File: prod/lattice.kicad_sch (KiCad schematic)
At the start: 65 parts, among them J1 USB_C_Receptacle, J2 USB_C_Receptacle, J3 AudioJack4, U1 XC6206PxxxMR, U2 USBLC6-2SC6, U3 CH552T

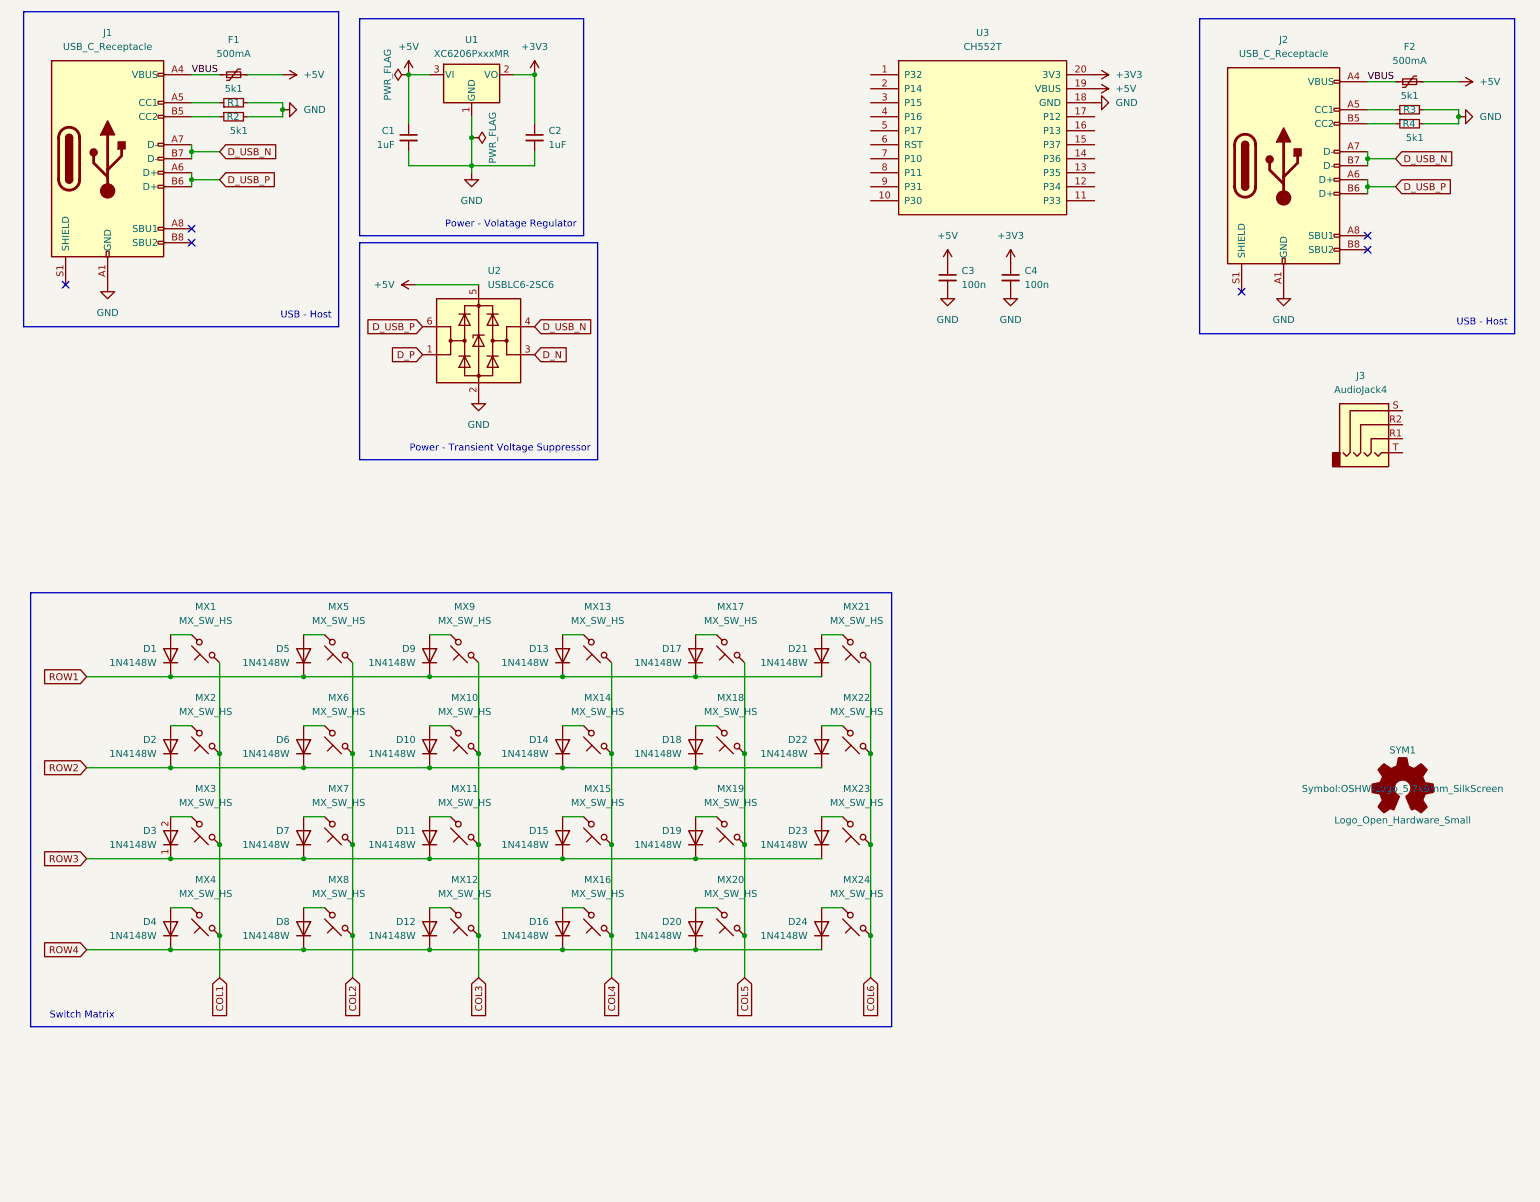
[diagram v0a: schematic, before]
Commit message: more complete schematic
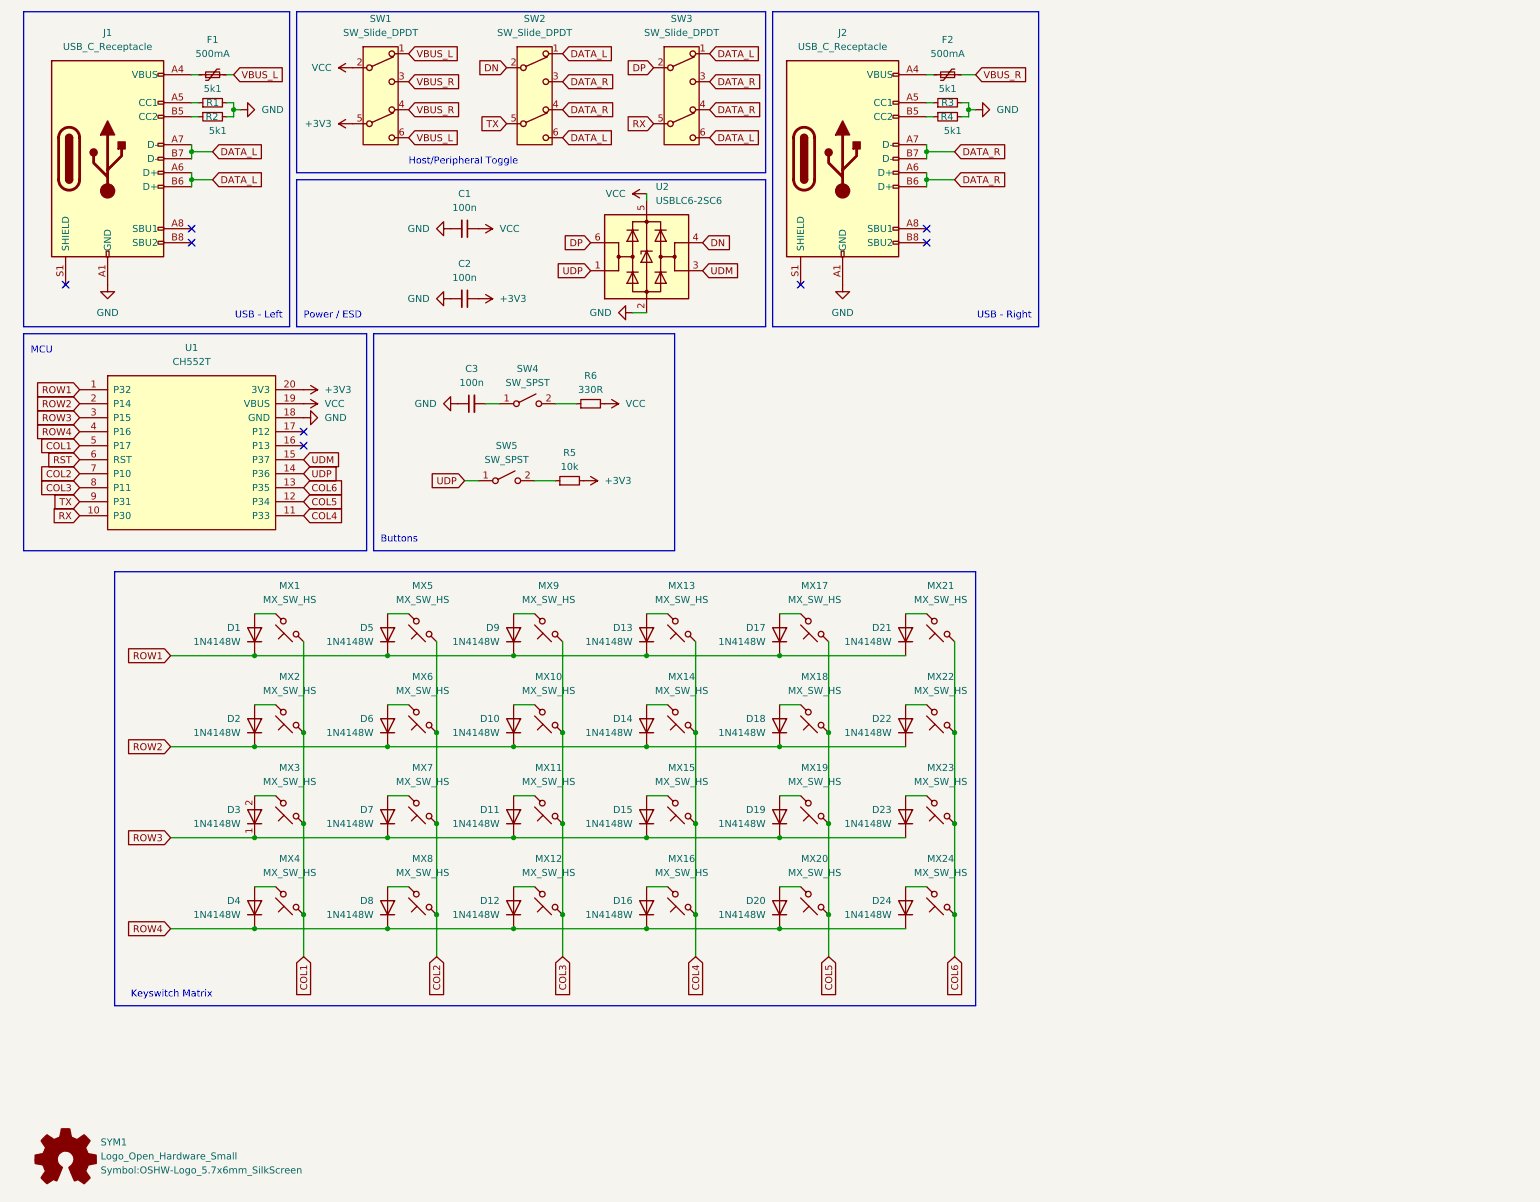
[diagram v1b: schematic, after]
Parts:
- removed C1, C2: 1uF, Capacitor_SMD:C_0402_1005Metric, symbol Device:C_Small
- removed J3: AudioJack4, symbol Connector_Audio:AudioJack4
- removed U1: XC6206PxxxMR, lattice:SOT-23-3, symbol Regulator_Linear:XC6206PxxxMR
- added C3: 100n, symbol Device:C_Small
- added R5: 10k, symbol Device:R_Small
- added R6: 330R, symbol Device:R_Small
- added SW1, SW2, SW3: SW_Slide_DPDT, symbol lattice:SW_Slide_DPDT
- added SW4, SW5: SW_SPST, symbol Switch:SW_SPST
- J1, J2: footprint lattice:USB_C_Receptacle_HRO_TYPE-C-31-M-12 -> Connector_USB:USB_C_Receptacle_HRO_TYPE-C-31-M-12
- MX1, MX10, MX11, MX12, MX13, MX14, MX15, MX16, MX17, MX18, MX19, MX2, MX20, MX21, MX22, MX23, MX24, MX3, MX4, MX5, MX6, MX7, MX8, MX9: footprint siderakb/key-switches:SW_Gateron_LowProfile_HotSwap_PTH -> marbastlib-choc:SW_choc_v1_HS_1u
- renumbered C3 to C1, C4 to C2, U3 to U1
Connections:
- net D_N is gone; now on net UDM: U2.3 (I/O2)
- net D_P is gone; now on net UDP: U2.1 (I/O1)
- net +3V3: now also R5.2, SW1.5
- net COL1: now also U1.5 (P17)
- net COL2: now also U1.7 (P10)
- net COL3: now also U1.8 (P11)
- net COL4: now also U1.11 (P33)
- net COL5: now also U1.12 (P34)
- net COL6: now also U1.13 (P35)
- net GND: now also C3.1
- net ROW1: now also U1.1 (P32)
- net ROW2: now also U1.2 (P14)
- net ROW3: now also U1.3 (P15)
- net ROW4: now also U1.4 (P16)
- net RX: now reaches U1.10 (P30)
- net RX: now also SW3.5
- net UDP: now reaches U1.14 (P36)
- net UDP: now also SW5.1 (A)
- net UDM: now reaches U1.15 (P37)
- net RST: now reaches U1.6 (RST)
- net TX: now reaches U1.9 (P31)
- net TX: now also SW2.5
- net +5V renamed VCC
- net VCC: now also R6.2, SW1.2; no longer F1.2, F2.2
- removed net D_USB_N: J1.A7 (D-), J1.B7 (D-), J2.A7 (D-), J2.B7 (D-), U2.4 (I/O2)
- removed net D_USB_P: J1.A6 (D+), J1.B6 (D+), J2.A6 (D+), J2.B6 (D+), U2.6 (I/O1)
- net VBUS: no longer names the net of F2.1, J2.A4 (VBUS), J2.A9 (VBUS), J2.B4 (VBUS), J2.B9 (VBUS)
- net VBUS: no longer F1.1, J1.A4 (VBUS), J1.A9 (VBUS), J1.B4 (VBUS), J1.B9 (VBUS)
- new net: C3.2, SW4.1 (A)
- new net: R6.1, SW4.2 (B)
- new net: F1.1, J1.A4 (VBUS), J1.A9 (VBUS), J1.B4 (VBUS), J1.B9 (VBUS)
- new net: R5.1, SW5.2 (B)
- new net DATA_L: J1.A6 (D+), J1.A7 (D-), J1.B6 (D+), J1.B7 (D-), SW2.1, SW2.6, SW3.1, SW3.6
- new net DATA_R: J2.A6 (D+), J2.A7 (D-), J2.B6 (D+), J2.B7 (D-), SW2.3, SW2.4, SW3.3, SW3.4
- new net DN: SW2.2, U2.4 (I/O2)
- new net DP: SW3.2, U2.6 (I/O1)
- new net VBUS_L: F1.2, SW1.1, SW1.6
- new net VBUS_R: F2.2, SW1.3, SW1.4
- no-connect marks 6 -> 8
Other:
- note added: "Buttons"
- note added: "Host/Peripheral Toggle"
- note added: "Keyswitch Matrix"
- note added: "MCU"
- note added: "Power / ESD"
- note added: "USB - Left"
- note added: "USB - Right"
- note removed: "Power - Transient Voltage Suppressor"
- note removed: "Power - Volatage Regulator"
- note removed: "Switch Matrix"
- note removed: "USB - Host"
- moved on the sheet: C1, C2, D1, D10, D11, D12, D13, D14, D15, D16, D17, D18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

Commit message: schematic work
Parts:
- B1: renamed from SW4; footprint (none) -> project:SW_SPST_SKQG_WithStem; symbol Switch:SW_SPST -> lattice:SW_SPST
- B2: renamed from SW5; footprint (none) -> project:SW_SPST_SKQG_WithStem; symbol Switch:SW_SPST -> lattice:SW_SPST
- C1: renamed from C3; footprint (none) -> project:C_0603_1608Metric; symbol Device:C_Small -> lattice:C_Small
- C2: renamed from C1; footprint Capacitor_SMD:C_0402_1005Metric -> project:C_0603_1608Metric; symbol Device:C_Small -> lattice:C_Small
- C3: renamed from C2; footprint Capacitor_SMD:C_0402_1005Metric -> project:C_0603_1608Metric; symbol Device:C_Small -> lattice:C_Small
- D1: symbol Diode:1N4148W -> lattice:1N4148W_1
- D10, D11, D12, D13, D14, D15, D16, D17, D18, D19, D2, D20, D21, D22, D23, D24, D4, D5, D6, D7, D8, D9: symbol Diode:1N4148W -> lattice:1N4148W
- D3: symbol Diode:1N4148W -> lattice:1N4148W_2
- F1, F2: footprint Fuse:Fuse_0402_1005Metric -> project:Fuse_0603_1608Metric; symbol Device:Polyfuse_Small -> lattice:Polyfuse_Small
- J1, J2: footprint Connector_USB:USB_C_Receptacle_HRO_TYPE-C-31-M-12 -> project:USB_C_Receptacle_HRO_TYPE-C-31-M-12; symbol Connector:USB_C_Receptacle_USB2.0_16P -> lattice:USB_C_Receptacle_USB2.0_16P
- MX1: footprint marbastlib-choc:SW_choc_v1_HS_1u -> project:SW_MX_HS_S_1u; symbol marbastlib-mx:MX_SW_HS -> lattice:MX_SW_HS_1
- MX10, MX11, MX12, MX13, MX14, MX15, MX16, MX17, MX18, MX19, MX2, MX20, MX21, MX22, MX23, MX24, MX3, MX4, MX5, MX6, MX7, MX8, MX9: footprint marbastlib-choc:SW_choc_v1_HS_1u -> project:SW_MX_HS_S_1u; symbol marbastlib-mx:MX_SW_HS -> lattice:MX_SW_HS
- R1, R2: footprint Resistor_SMD:R_0402_1005Metric -> project:R_0603_1608Metric; symbol Device:R_Small -> lattice:R_Small
- R3: renamed from R6; footprint (none) -> project:R_0603_1608Metric; symbol Device:R_Small -> lattice:R_Small
- R4: renamed from R5; footprint (none) -> project:R_0603_1608Metric; symbol Device:R_Small -> lattice:R_Small
- R5: renamed from R3; footprint Resistor_SMD:R_0402_1005Metric -> project:R_0603_1608Metric; symbol Device:R_Small -> lattice:R_Small
- R6: renamed from R4; footprint Resistor_SMD:R_0402_1005Metric -> project:R_0603_1608Metric; symbol Device:R_Small -> lattice:R_Small
- SW1: renamed from SW2; footprint (none) -> project:SW_452403012014; Availability (none) -> In Stock; Check_prices (none) -> https://www.snapeda.com/parts/452403012014/Wurth+Electronic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; MANUFACTURER (none) -> Wurth Electronics; MAXIMUM_PACKAGE_HEIGHT (none) -> 3.3mm; MF (none) -> Wurth Electronics; MP (none) -> 452403012014; PARTREV (none) -> 001.001; Package (none) -> None; Price (none) -> None; Purchase-URL (none) -> https://www.snapeda.com/api/url_track_click_mouser/?unipart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; SNAPEDA_PN (none) -> 452403012014; STANDARD (none) -> Manufacturer Recommendations; SnapEDA_Link (none) -> https://www.snapeda.com/parts/452403012014/Wurth+Electronic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
- SW2: renamed from SW1; footprint (none) -> project:SW_452403012014; Availability (none) -> In Stock; Check_prices (none) -> https://www.snapeda.com/parts/452403012014/Wurth+Electronic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; MANUFACTURER (none) -> Wurth Electronics; MAXIMUM_PACKAGE_HEIGHT (none) -> 3.3mm; MF (none) -> Wurth Electronics; MP (none) -> 452403012014; PARTREV (none) -> 001.001; Package (none) -> None; Price (none) -> None; Purchase-URL (none) -> https://www.snapeda.com/api/url_track_click_mouser/?unipart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; SNAPEDA_PN (none) -> 452403012014; STANDARD (none) -> Manufacturer Recommendations; SnapEDA_Link (none) -> https://www.snapeda.com/parts/452403012014/Wurth+Electronic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
- SW3: footprint (none) -> project:SW_452403012014; Availability (none) -> In Stock; Check_prices (none) -> https://www.snapeda.com/parts/452403012014/Wurth+Electronic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; MANUFACTURER (none) -> Wurth Electronics; MAXIMUM_PACKAGE_HEIGHT (none) -> 3.3mm; MF (none) -> Wurth Electronics; MP (none) -> 452403012014; PARTREV (none) -> 001.001; Package (none) -> None; Price (none) -> None; Purchase-URL (none) -> https://www.snapeda.com/api/url_track_click_mouser/?unipart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; SNAPEDA_PN (none) -> 452403012014; STANDARD (none) -> Manufacturer Recommendations; SnapEDA_Link (none) -> https://www.snapeda.com/parts/452403012014/Wurth+Electronic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
- SYM1: footprint Symbol:OSHW-Logo_5.7x6mm_SilkScreen -> project:OSHW-Logo_5.7x6mm_SilkScreen; symbol Graphic:Logo_Open_Hardware_Small -> lattice:Logo_Open_Hardware_Small
- U1: footprint Package_SO:TSSOP-20-1EP_4.4x6.5mm_P0.65mm_EP2.15x3.35mm -> project:TSSOP-20_4.4x6.5mm_P0.65mm; symbol rgoulter:CH552T -> lattice:CH552T
- U2: footprint Package_TO_SOT_SMD:SOT-23-6 -> project:SOT-23-6; symbol Power_Protection:USBLC6-2SC6 -> lattice:USBLC6-2SC6
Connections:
- net RST: now also B1.1 (A), C1.2
- net TX: now also SW1.2; no longer SW1.5
- net VBUS_L: now also SW2.3, SW2.4; no longer SW2.1, SW2.6
- net VBUS_R: now also SW2.1, SW2.6; no longer SW2.3, SW2.4
- removed net DATA_L: J1.A6 (D+), J1.A7 (D-), J1.B6 (D+), J1.B7 (D-), SW1.1, SW1.6, SW3.1, SW3.6
- removed net DATA_R: J2.A6 (D+), J2.A7 (D-), J2.B6 (D+), J2.B7 (D-), SW1.3, SW1.4, SW3.3, SW3.4
- net DN renamed DM
- net DM: now also SW1.5; no longer SW1.2
- new net DM_L: J1.A7 (D-), J1.B7 (D-), SW1.3, SW1.4
- new net DM_R: J2.A7 (D-), J2.B7 (D-), SW1.1, SW1.6
- new net DP_L: J1.A6 (D+), J1.B6 (D+), SW3.3, SW3.4
- new net DP_R: J2.A6 (D+), J2.B6 (D+), SW3.1, SW3.6
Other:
- note added: "Host / Peripheral Toggle"
- note added: "USB Left"
- note added: "USB Right"
- note removed: "Buttons"
- note removed: "Host/Peripheral Toggle"
- note removed: "USB - Left"
- note removed: "USB - Right"
- title: lattice (left) -> lattice
- moved on the sheet: B1, B2, C1, C2, C3, D1, D10, D11, D12, D13, D14, D15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

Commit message: schematic pretty solid
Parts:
- SW1, SW2, SW3: footprint project:SW_452403012014 -> project:K3_1390S
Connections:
- net DM: now also SW1.2; no longer SW1.5
- net TX: now also SW1.5; no longer SW1.2
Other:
- note added: "Boot"
- note added: "Reset"
- moved on the sheet: F2, J2, R5, R6, SW1, SW2, SW3, U1
